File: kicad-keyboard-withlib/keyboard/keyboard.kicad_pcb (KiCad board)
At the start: 2 copper layers, 200.5 x 128.5 mm, 47 parts, among them SW1 SW_Push, SW10 SW_Push, SW11 SW_Push, SW12 SW_Push, SW13 SW_Push, SW14 SW_Push, SW15 SW_Push, SW16 SW_Push, SW17 SW_Push, SW18 SW_Push, SW19 SW_Push, SW2 SW_Push, SW20 SW_Push, SW21 SW_Push, SW22 SW_Push, SW23 SW_Push, SW24 SW_Push, SW25 SW_Push, SW26 SW_Push, SW27 SW_Push, SW28 SW_Push, SW29 SW_Push, SW3 SW_Push, SW30 SW_Push, SW31 SW_Push, SW32 SW_Push, SW33 SW_Push, SW34 SW_Push, SW35 SW_Push, SW36 SW_Push, SW37 SW_Push, SW38 SW_Push, SW39 SW_Slide_DPDT, SW4 SW_Push, SW5 SW_Push, SW6 SW_Push, SW7 SW_Push, SW8 SW_Push, SW9 SW_Push, U2 MCP23017_SO

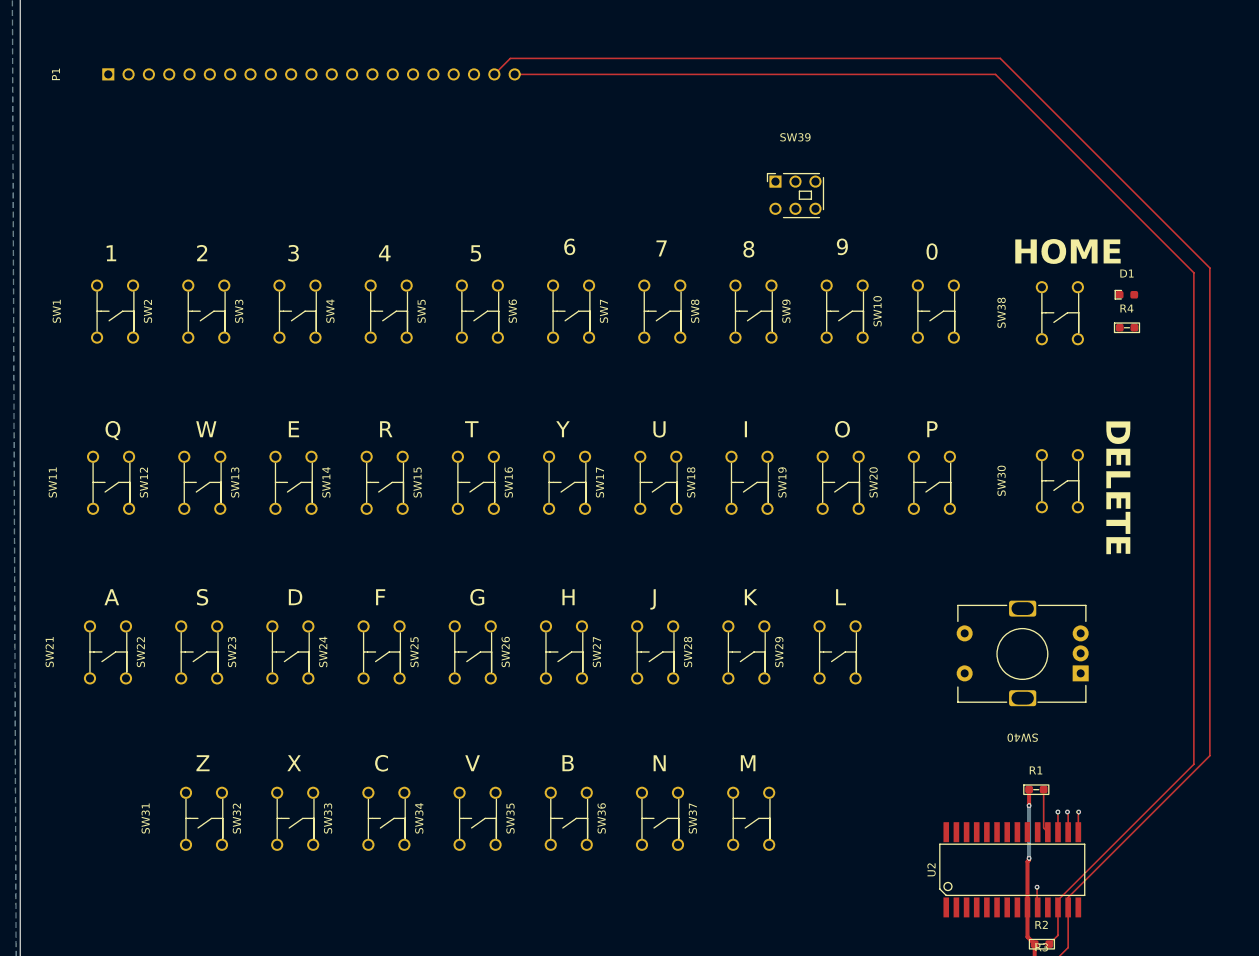
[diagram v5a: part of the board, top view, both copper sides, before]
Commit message: add: new male header
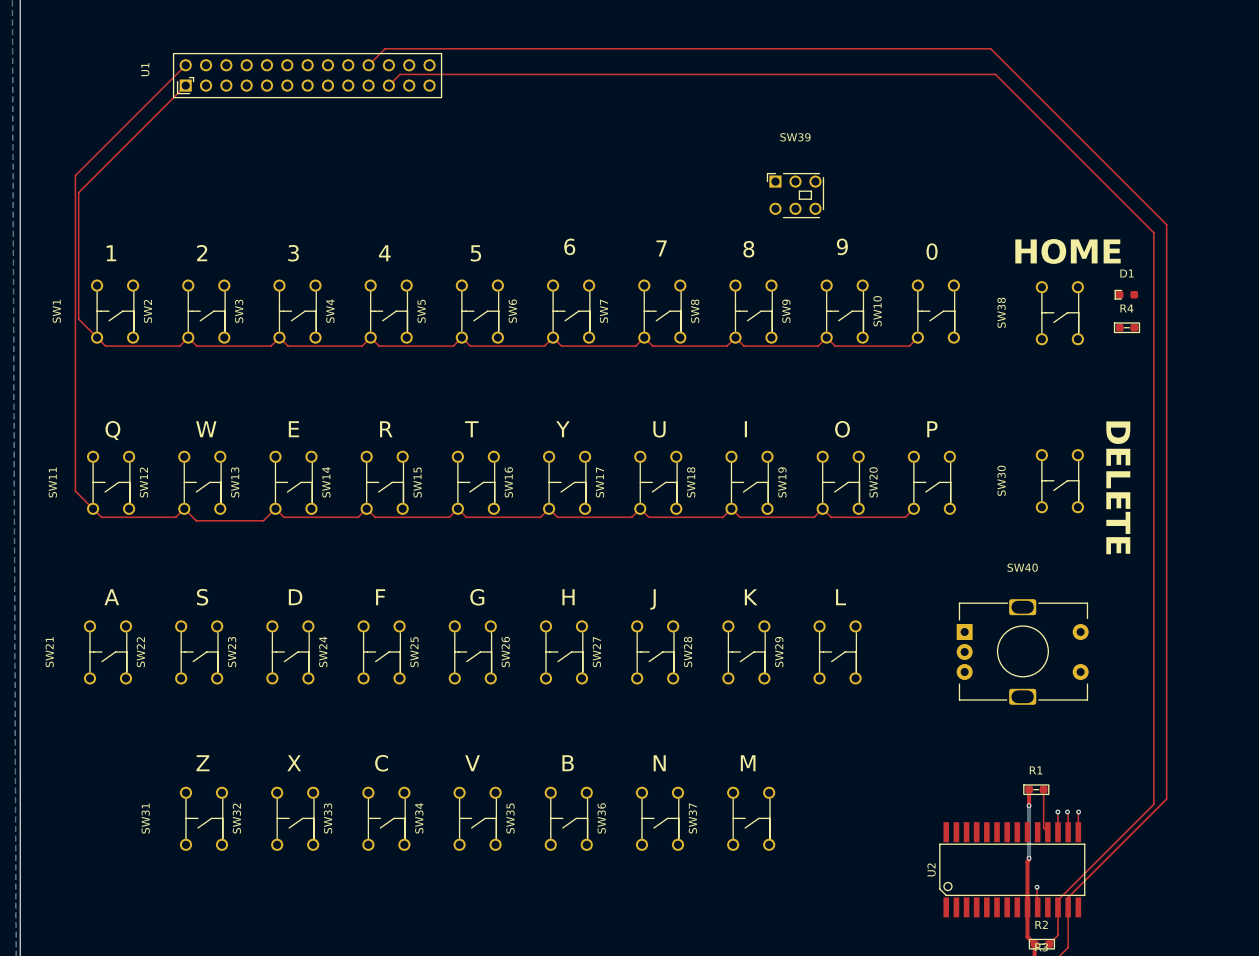
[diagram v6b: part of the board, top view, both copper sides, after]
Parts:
- removed P1: ~, Lilyspad:pin_socket
- added U1: ~, Lilyspad:male_header, F.Cu at (40.7, 48.8)
- moved SW40 20.2 mm to (149.8, 111.6), turned to 0 degrees
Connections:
- SW40 pad D: (no net) -> GND
- SW40 pad E: (no net) -> Net-(U2-GPA5)
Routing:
- net Net-(U1-R2): track 0.00 -> 172.9 mm
- net Net-(U1-R1): track 0.00 -> 148.5 mm
- net Net-(U1-SCL): track 186.6 -> 198.7 mm
- net Net-(U1-SDA): track 196.7 -> 208.5 mm

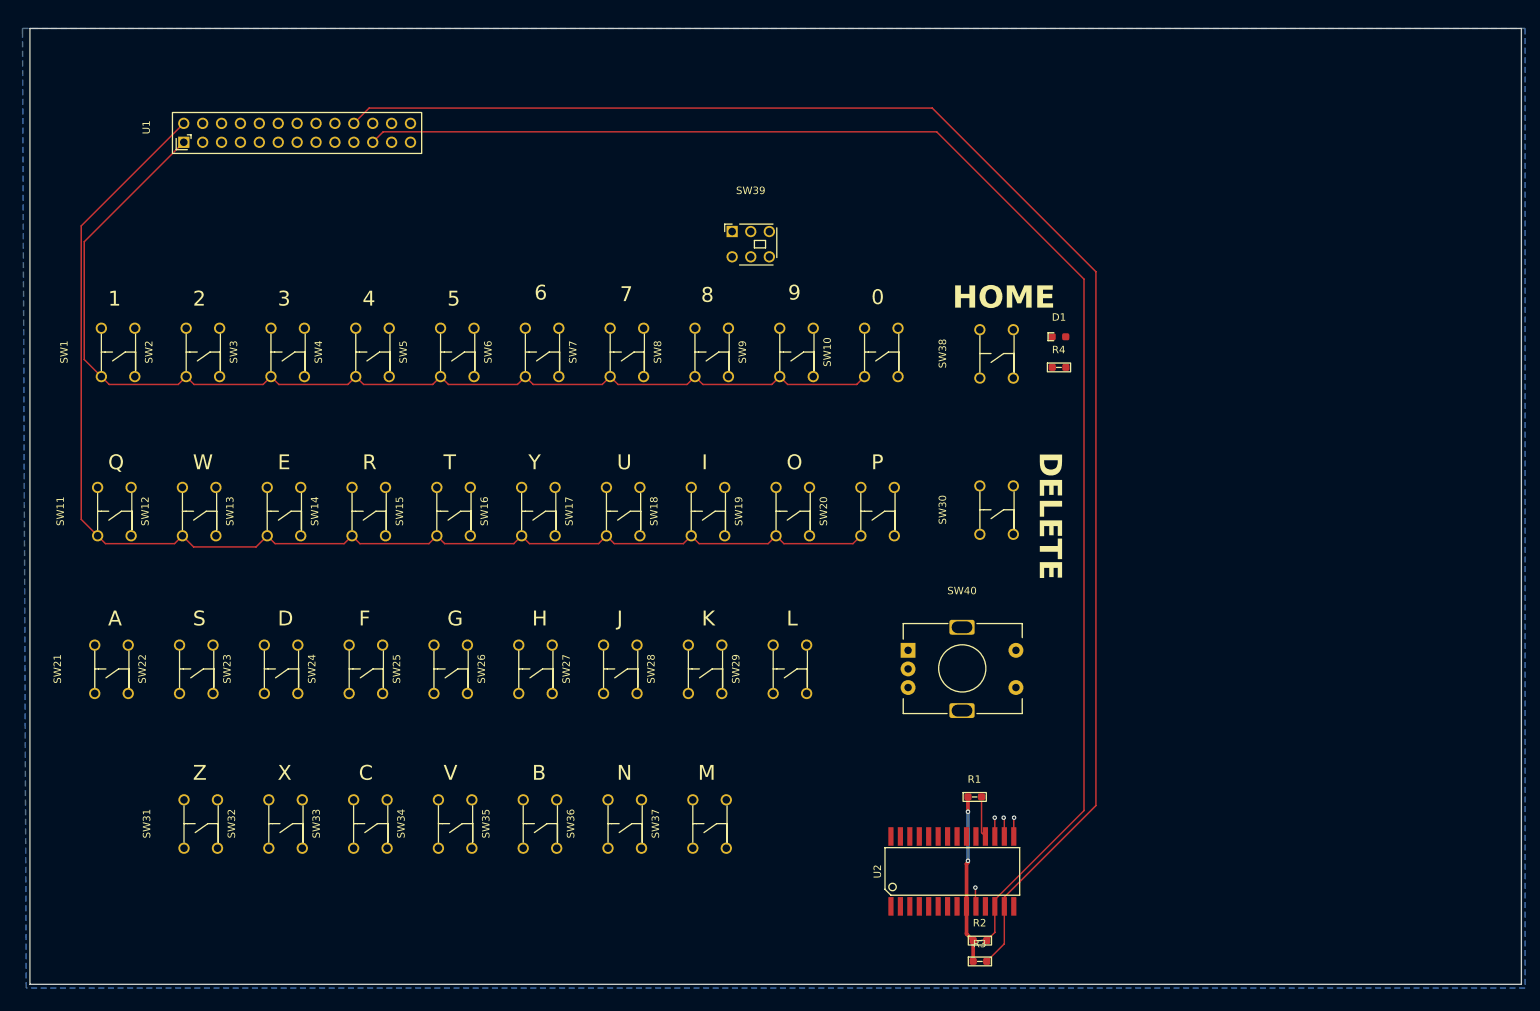
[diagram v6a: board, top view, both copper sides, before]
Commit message: add: brand new pcb for the keyboard
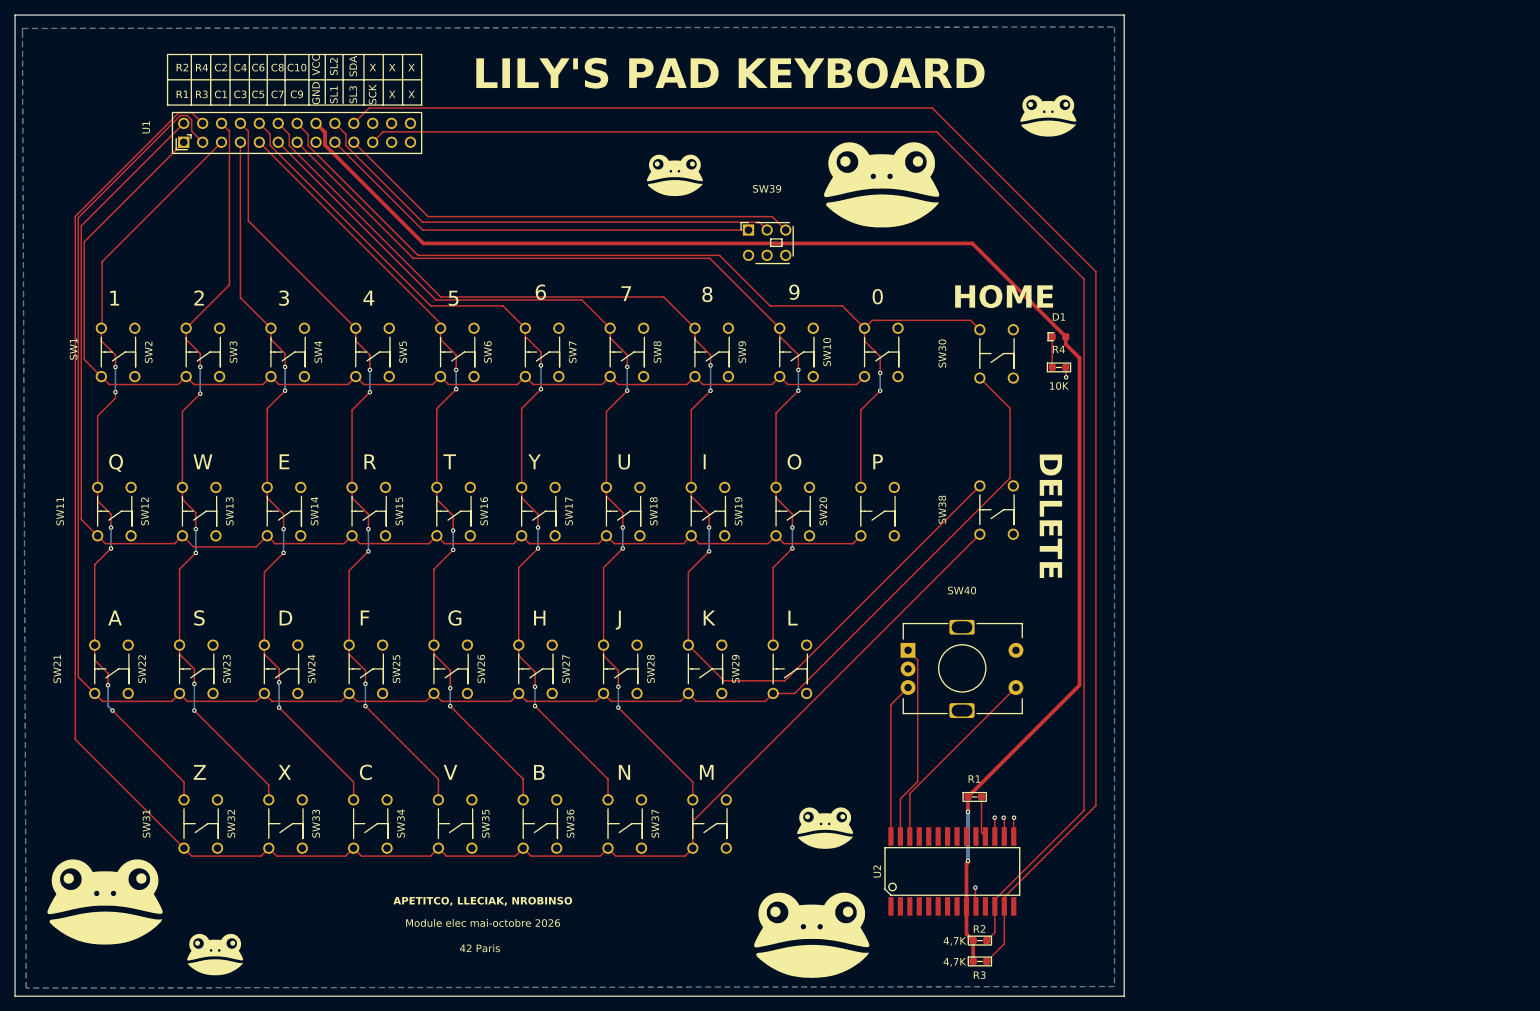
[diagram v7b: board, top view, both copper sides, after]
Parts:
- added G***: LOGO, LOGO, F.Cu at (161.4, 46.8)
- added G***: LOGO, LOGO, F.Cu at (34.6, 152.0)
- added G***: LOGO, LOGO, F.Cu at (139.0, 55.6)
- added G***: LOGO, LOGO, F.Cu at (49.4, 159.5)
- added G***: LOGO, LOGO, F.Cu at (131.4, 142.5)
- added G***: LOGO, LOGO, F.Cu at (111.2, 54.8)
- added G***: LOGO, LOGO, F.Cu at (129.6, 156.5)
- moved SW30 21.0 mm to (147.7, 79.2)
- moved SW38 21.0 mm to (147.7, 100.2)
- moved SW39 2.21 mm to (123.6, 57.6)
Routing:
- net Net-(U1-R3): track 0.00 -> 246.9 mm
- net Net-(U1-R4): track 0.00 -> 246.4 mm
- net VCC: track 22.6 -> 205.1 mm
- net Net-(U1-C8): track 0.00 -> 167.0 mm, vias 0 -> 4
- net Net-(U1-C10): track 0.00 -> 128.4 mm, vias 0 -> 2
- net Net-(U1-C7): track 0.00 -> 127.6 mm, vias 0 -> 6
- net Net-(U1-C9): track 0.00 -> 122.1 mm, vias 0 -> 4
- net Net-(U1-C6): track 0.00 -> 120.3 mm, vias 0 -> 6
- net Net-(U1-C5): track 0.00 -> 107.6 mm, vias 0 -> 6
- net Net-(U1-C4): track 0.00 -> 106.1 mm, vias 0 -> 6
- net Net-(U1-C1): track 0.00 -> 103.5 mm, vias 0 -> 6
- net Net-(U1-C2): track 0.00 -> 102.2 mm, vias 0 -> 6
- net Net-(U1-C3): track 0.00 -> 98.8 mm, vias 0 -> 6
- net Net-(SW39-B-Pad2): track 0.00 -> 64.9 mm
- net Net-(SW39-C-Pad3): track 0.00 -> 62.9 mm
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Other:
- board size 200.5 x 128.5 mm -> 149.1 x 131.9 mm
- board text added: "10K"
- board text added: "4,7K"
- board text added: "42 Paris"
- board text added: "APETITCO, LLECIAK, NROBINSO"
- board text added: "C1"
- board text added: "C10"
- board text added: "C2"
- board text added: "C3"
- board text added: "C4"
- board text added: "C5"
- board text added: "C6"
- board text added: "C7"
- board text added: "C8"
- board text added: "C9"
- board text added: "GND"
- board text added: "LILY'S PAD KEYBOARD"
- board text added: "Module elec mai-octobre 2026"
- board text added: "R1"
- board text added: "R2"
- board text added: "R3"
- board text added: "R4"
- board text added: "SCK"
- board text added: "SDA"
- board text added: "SL1"
- board text added: "SL2"
- board text added: "SL3"
- board text added: "VCC"
